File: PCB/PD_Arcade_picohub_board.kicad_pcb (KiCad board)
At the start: 2 copper layers, 75 x 82.3 mm, 33 parts, among them J1 Partition_Lights_L, J10 Circle_LED, J11 Cross_LED, J12 Square_LED, J13 Triangle_LED, J14 Slider LEDs 5V power, J15 5V_In, J2 Start_button, J3 12V_In, J4 Circle_button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

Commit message: PCB readme
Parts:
- JP2: renamed from ←Short if there is no PWM 
- JP4: renamed from ↓Short if there is no PWM 
- renumbered U3 to U1, U6 to U3, U1 to U4

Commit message: README.md and PCB update
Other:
- board text added: "←Short if no PWM used"
- board text added: "↓Short if no PWM used"
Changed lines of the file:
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@@
     (property "ki_keywords" "solder jumper SPST")
     (attr exclude_from_pos_files)
-    (fp_text reference "JP2" (at 2.174 -0.762 180) (layer "F.SilkS")
+    (fp_text reference "JP2" (at 2.174 -0.762 180) (layer "F.SilkS") hide
       (effects (font (size 1 0.3) (thickness 0.075) bold))
     )
@@
     (property "ki_keywords" "solder jumper SPST")
     (attr exclude_from_pos_files)
-    (fp_text reference "JP4" (at 2.428 0.508) (layer "B.SilkS")
+    (fp_text reference "JP4" (at 2.428 0.508) (layer "B.SilkS") hide
       (effects (font (size 1 0.3) (thickness 0.075)) (justify mirror))
     )
@@
   (gr_rect (start 247.142 40.903751) (end 270.023751 58.24)
     (stroke (width 0.15) (type default)) (fill none) (layer "F.SilkS"))
-  (gr_rect (start 210.82 107.95) (end 217.424 112.776)
+  (gr_rect (start 210.82 107.95) (end 216.408 112.776)
     (stroke (width 0.15) (type default)) (fill none) (layer "F.SilkS"))
   (gr_rect (start 204.392 40.728) (end 279.384 123.068)
     (stroke (width 0.1) (type default)) (fill none) (layer "Edge.Cuts"))
+  (gr_text "↓Short if no PWM used" (at 216.154 112.776) (layer "B.SilkS")
+    (effects (font (size 1 0.3) (thickness 0.075)) (justify left bottom mirror))
+  )
   (gr_text "12V G   R   B" (at 214.576 89.916 90) (layer "F.SilkS")
     (effects (font (size 1 0.8) (thickness 0.2) bold) (justify bottom))
@@
     (effects (font (size 3 3) (thickness 0.4)) (justify left bottom))
   )
+  (gr_text "←Short if no PWM used" (at 210.82 112.776) (layer "F.SilkS")
+    (effects (font (size 1 0.3) (thickness 0.075)) (justify left bottom))
+  )
   (gr_text "TX RX -  +" (at 250.622 50.592 -90) (layer "F.SilkS")

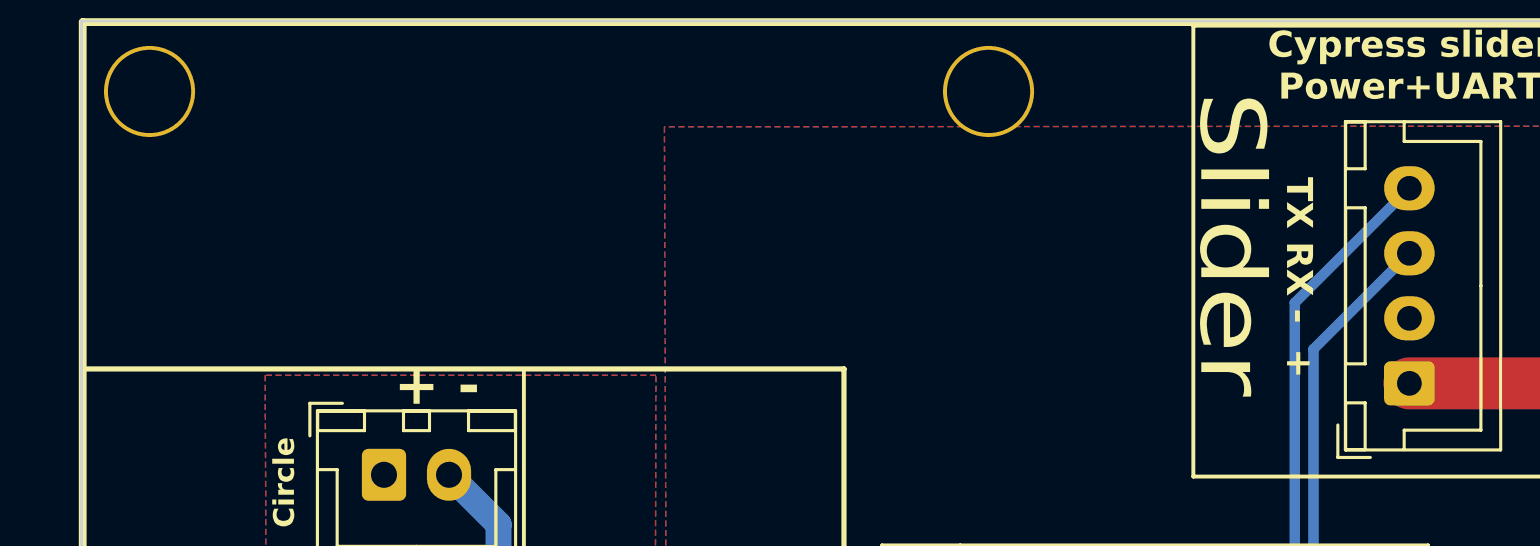
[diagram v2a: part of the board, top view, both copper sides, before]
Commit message: README.md update
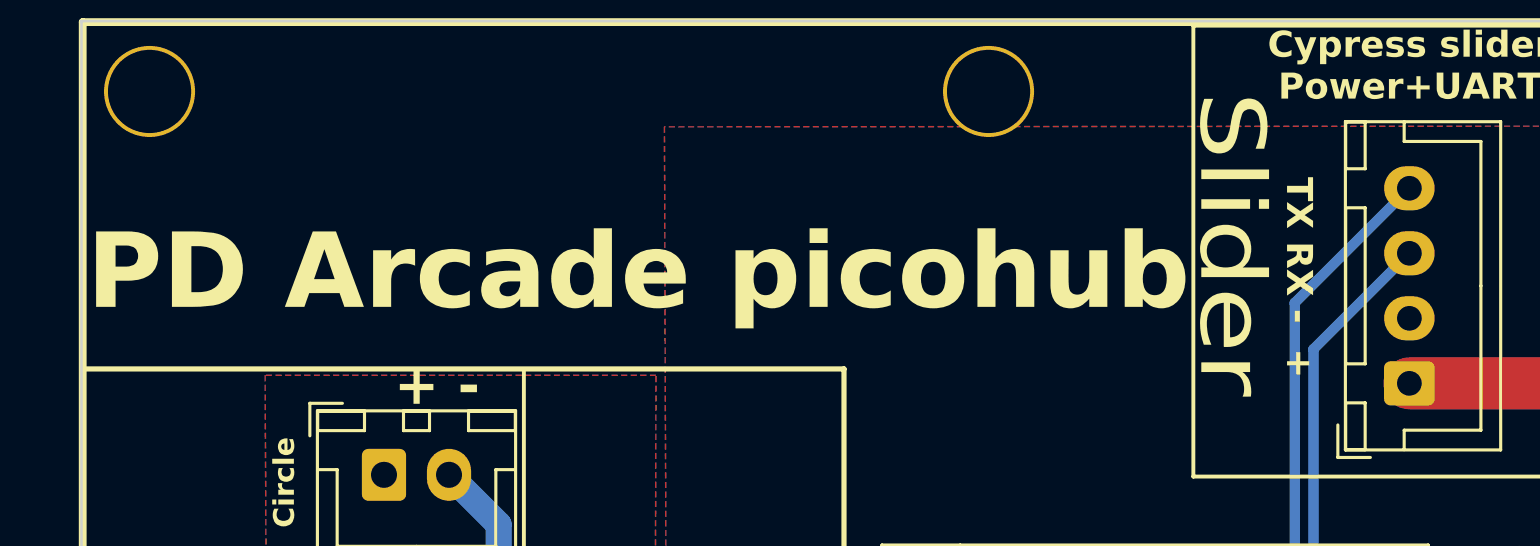
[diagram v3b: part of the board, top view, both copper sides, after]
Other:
- board text added: "PD Arcade picohub"
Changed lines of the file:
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@@
     (effects (font (size 2.5 3) (thickness 0.4)) (justify left bottom))
+  )
+  (gr_text "PD Arcade picohub" (at 204.59 52.07) (layer "F.SilkS")
+    (effects (font (size 2.9 2.9) (thickness 0.4) bold) (justify left bottom))
   )
   (gr_text "Start" (at 272.878 91.466 -90) (layer "F.SilkS")

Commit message: R1 fix to 1k
10k do not work
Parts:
- R1: value 10k -> 1k
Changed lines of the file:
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@@
       (effects (font (size 1 1) (thickness 0.15)))
     )
-    (fp_text value "10k" (at 0 1.82 -180) (layer "F.Fab")
+    (fp_text value "1k" (at 0 1.82 -180) (layer "F.Fab")
       (effects (font (size 1 1) (thickness 0.15)))
     )
